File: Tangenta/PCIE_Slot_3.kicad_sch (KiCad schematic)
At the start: 10 parts, among them J20 10018784-10213TLF

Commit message: M2_Slot, PCIE_x16_Slot, PCIE_Switch
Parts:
- J20: footprint PCIE_x16_Slot:PCIE_x16_Slot -> CholaFootprintsPrjLib:PCIE_x16_Slot
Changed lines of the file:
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@@
       (effects (font (size 1.27 1.27)))
     )
-    (property "Footprint" "PCIE_x16_Slot:PCIE_x16_Slot" (at 218.44 154.635 0)
+    (property "Footprint" "CholaFootprintsPrjLib:PCIE_x16_Slot" (at 218.44 154.635 0)
       (effects (font (size 1.27 1.27)) (justify left top) hide)
     )

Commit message: CAP_L6, CAP_TANTAL_A, M24C04-RMN6TP
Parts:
- C114, C115: footprint CAP_L6:CAP_L6 -> CholaFootprintsPrjLib:CAP_L6
- C116, C117: footprint CAP_TANTAL_A:CAP_TANTAL_A -> CholaFootprintsPrjLib:CAP_TANTAL_A
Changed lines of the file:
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@@
       (effects (font (size 1.27 1.27)) (justify right))
     )
-    (property "Footprint" "CAP_TANTAL_A:CAP_TANTAL_A" (at 203.581 260.477 0)
+    (property "Footprint" "CholaFootprintsPrjLib:CAP_TANTAL_A" (at 203.581 260.477 0)
       (effects (font (size 1.27 1.27) italic) hide)
     )
@@
     )
   )
-  (symbol (lib_id "CholaSymbolsPrjLib:35CE47AX") (at 203.2 263.525 0) (unit 1)
+  (symbol (lib_name "35CE47AX_1") (lib_id "CholaSymbolsPrjLib:35CE47AX") (at 203.2 263.525 0) (unit 1)
     (in_bom yes) (on_board yes) (dnp no)
     (property "Reference" "C115" (at 205.105 262.255 0)
@@
       (effects (font (size 1.27 1.27)) (justify left))
     )
-    (property "Footprint" "CAP_L6:CAP_L6" (at 206.248 282.575 0)
+    (property "Footprint" "CholaFootprintsPrjLib:CAP_L6" (at 206.248 282.575 0)
       (effects (font (size 1.27 1.27) italic) hide)
     )
@@
     )
   )
-  (symbol (lib_id "CholaSymbolsPrjLib:CA45-A-6_3V-47UF-K") (at 226.06 263.525 270) (mirror x) (unit 1)
+  (symbol (lib_name "CA45-A-6_3V-47UF-K_1") (lib_id "CholaSymbolsPrjLib:CA45-A-6_3V-47UF-K") (at 226.06 263.525 270) (mirror x) (unit 1)
     (in_bom yes) (on_board yes) (dnp no)
     (property "Reference" "C117" (at 233.68 262.255 90)
@@
       (effects (font (size 1.27 1.27)) (justify right))
     )
-    (property "Footprint" "CAP_TANTAL_A:CAP_TANTAL_A" (at 214.376 260.477 0)
+    (property "Footprint" "CholaFootprintsPrjLib:CAP_TANTAL_A" (at 214.376 260.477 0)
       (effects (font (size 1.27 1.27) italic) hide)
     )
@@
       (effects (font (size 1.27 1.27)) (justify left))
     )
-    (property "Footprint" "CAP_L6:CAP_L6" (at 196.088 282.575 0)
+    (property "Footprint" "CholaFootprintsPrjLib:CAP_L6" (at 196.088 282.575 0)
       (effects (font (size 1.27 1.27) italic) hide)
     )

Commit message: Removing component association with previous project (local) libraries.
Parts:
- C114, C115: footprint CholaFootprintsPrjLib:CAP_L6 -> CAP_L6:CAP_L6; symbol CholaSymbolsPrjLib:35CE47AX -> 35CE47AX:35CE47AX
- C116, C117: footprint CholaFootprintsPrjLib:CAP_TANTAL_A -> CAP_TANTAL_A:CAP_TANTAL_A; symbol CholaSymbolsPrjLib:CA45-A-6_3V-47UF-K -> CA45-A-6_3V-47UF-K:CA45-A-6_3V-47UF-K
- J20: footprint CholaFootprintsPrjLib:PCIE_x16_Slot -> PCIE_x16_Slot:PCIE_x16_Slot; symbol CholaSymbolsPrjLib:10018784-10213TLF -> 10018784-10213TLF:10018784-10213TLF
- R88, R89, R90, R91: symbol CholaSymbolsPrjLib:R_Small_US -> R_Small_US:R_Small_US
- TP3: symbol CholaSymbolsPrjLib:TestPoint_Small -> TestPoint_Small:TestPoint_Small
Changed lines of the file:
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@@
 	)
 	(symbol
-		(lib_id "CholaSymbolsPrjLib:R_Small_US")
+		(lib_id "R_Small_US:R_Small_US")
 		(at 237.49 236.855 270)
 		(unit 1)
@@
 	)
 	(symbol
-		(lib_id "CholaSymbolsPrjLib:R_Small_US")
+		(lib_id "R_Small_US:R_Small_US")
 		(at 237.49 239.395 270)
 		(unit 1)
@@
 	)
 	(symbol
-		(lib_id "CholaSymbolsPrjLib:CA45-A-6_3V-47UF-K")
+		(lib_id "CA45-A-6_3V-47UF-K:CA45-A-6_3V-47UF-K")
 		(at 215.265 263.525 270)
 		(mirror x)
@@
 			)
 		)
-		(property "Footprint" "CholaFootprintsPrjLib:CAP_TANTAL_A"
+		(property "Footprint" "CAP_TANTAL_A:CAP_TANTAL_A"
 			(at 203.581 260.477 0)
 			(effects
@@
 	)
 	(symbol
-		(lib_id "CholaSymbolsPrjLib:10018784-10213TLF")
+		(lib_id "10018784-10213TLF:10018784-10213TLF")
 		(at 196.85 249.555 0)
 		(mirror x)
@@
 			)
 		)
-		(property "Footprint" "CholaFootprintsPrjLib:PCIE_x16_Slot"
+		(property "Footprint" "PCIE_x16_Slot:PCIE_x16_Slot"
 			(at 218.44 154.635 0)
 			(effects
@@
 	)
 	(symbol
-		(lib_id "CholaSymbolsPrjLib:R_Small_US")
+		(lib_id "R_Small_US:R_Small_US")
 		(at 34.29 45.72 270)
 		(unit 1)
@@
 	)
 	(symbol
-		(lib_id "CholaSymbolsPrjLib:R_Small_US")
+		(lib_id "R_Small_US:R_Small_US")
 		(at 241.935 203.2 0)
 		(unit 1)
@@
 	(symbol
 		(lib_name "35CE47AX_1")
-		(lib_id "CholaSymbolsPrjLib:35CE47AX")
+		(lib_id "35CE47AX:35CE47AX")
 		(at 203.2 263.525 0)
 		(unit 1)
@@
 			)
 		)
-		(property "Footprint" "CholaFootprintsPrjLib:CAP_L6"
+		(property "Footprint" "CAP_L6:CAP_L6"
 			(at 206.248 282.575 0)
 			(effects
@@
 	(symbol
 		(lib_name "CA45-A-6_3V-47UF-K_1")
-		(lib_id "CholaSymbolsPrjLib:CA45-A-6_3V-47UF-K")
+		(lib_id "CA45-A-6_3V-47UF-K:CA45-A-6_3V-47UF-K")
 		(at 226.06 263.525 270)
 		(mirror x)
@@
 			)
 		)
-		(property "Footprint" "CholaFootprintsPrjLib:CAP_TANTAL_A"
+		(property "Footprint" "CAP_TANTAL_A:CAP_TANTAL_A"
 			(at 214.376 260.477 0)
 			(effects
@@
 	)
 	(symbol
-		(lib_id "CholaSymbolsPrjLib:TestPoint_Small")
+		(lib_id "TestPoint_Small:TestPoint_Small")
 		(at 245.11 208.915 0)
 		(unit 1)
@@
 	)
 	(symbol
-		(lib_id "CholaSymbolsPrjLib:35CE47AX")
+		(lib_id "35CE47AX:35CE47AX")
 		(at 193.04 263.525 0)
 		(unit 1)
@@
 			)
 		)
-		(property "Footprint" "CholaFootprintsPrjLib:CAP_L6"
+		(property "Footprint" "CAP_L6:CAP_L6"
 			(at 196.088 282.575 0)
 			(effects

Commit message: Fixes, before checks.
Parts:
- C114, C115: symbol 35CE47AX:35CE47AX -> CAP_L6:35CE47AX
- C116, C117: symbol CA45-A-6_3V-47UF-K:CA45-A-6_3V-47UF-K -> CAP_TANTAL_A:CA45-A-6_3V-47UF-K
- J20: symbol 10018784-10213TLF:10018784-10213TLF -> PCIE_x16_Slot:10018784-10213TLF
- R88, R89, R90, R91: symbol R_Small_US:R_Small_US -> Device:R_Small_US
- TP3: symbol TestPoint_Small:TestPoint_Small -> Connector:TestPoint_Small
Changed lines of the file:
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@@
 	)
 	(symbol
-		(lib_id "R_Small_US:R_Small_US")
+		(lib_id "Device:R_Small_US")
 		(at 237.49 236.855 270)
 		(unit 1)
@@
 	)
 	(symbol
-		(lib_id "R_Small_US:R_Small_US")
+		(lib_id "Device:R_Small_US")
 		(at 237.49 239.395 270)
 		(unit 1)
@@
 	)
 	(symbol
-		(lib_id "CA45-A-6_3V-47UF-K:CA45-A-6_3V-47UF-K")
+		(lib_id "CAP_TANTAL_A:CA45-A-6_3V-47UF-K")
 		(at 215.265 263.525 270)
 		(mirror x)
@@
 	)
 	(symbol
-		(lib_id "10018784-10213TLF:10018784-10213TLF")
+		(lib_id "PCIE_x16_Slot:10018784-10213TLF")
 		(at 196.85 249.555 0)
 		(mirror x)
@@
 	)
 	(symbol
-		(lib_id "R_Small_US:R_Small_US")
+		(lib_id "Device:R_Small_US")
 		(at 34.29 45.72 270)
 		(unit 1)
@@
 	)
 	(symbol
-		(lib_id "R_Small_US:R_Small_US")
+		(lib_id "Device:R_Small_US")
 		(at 241.935 203.2 0)
 		(unit 1)
@@
 	(symbol
 		(lib_name "35CE47AX_1")
-		(lib_id "35CE47AX:35CE47AX")
+		(lib_id "CAP_L6:35CE47AX")
 		(at 203.2 263.525 0)
 		(unit 1)
@@
 	(symbol
 		(lib_name "CA45-A-6_3V-47UF-K_1")
-		(lib_id "CA45-A-6_3V-47UF-K:CA45-A-6_3V-47UF-K")
+		(lib_id "CAP_TANTAL_A:CA45-A-6_3V-47UF-K")
 		(at 226.06 263.525 270)
 		(mirror x)
@@
 	)
 	(symbol
-		(lib_id "TestPoint_Small:TestPoint_Small")
+		(lib_id "Connector:TestPoint_Small")
 		(at 245.11 208.915 0)
 		(unit 1)
@@
 	)
 	(symbol
-		(lib_id "35CE47AX:35CE47AX")
+		(lib_id "CAP_L6:35CE47AX")
 		(at 193.04 263.525 0)
 		(unit 1)

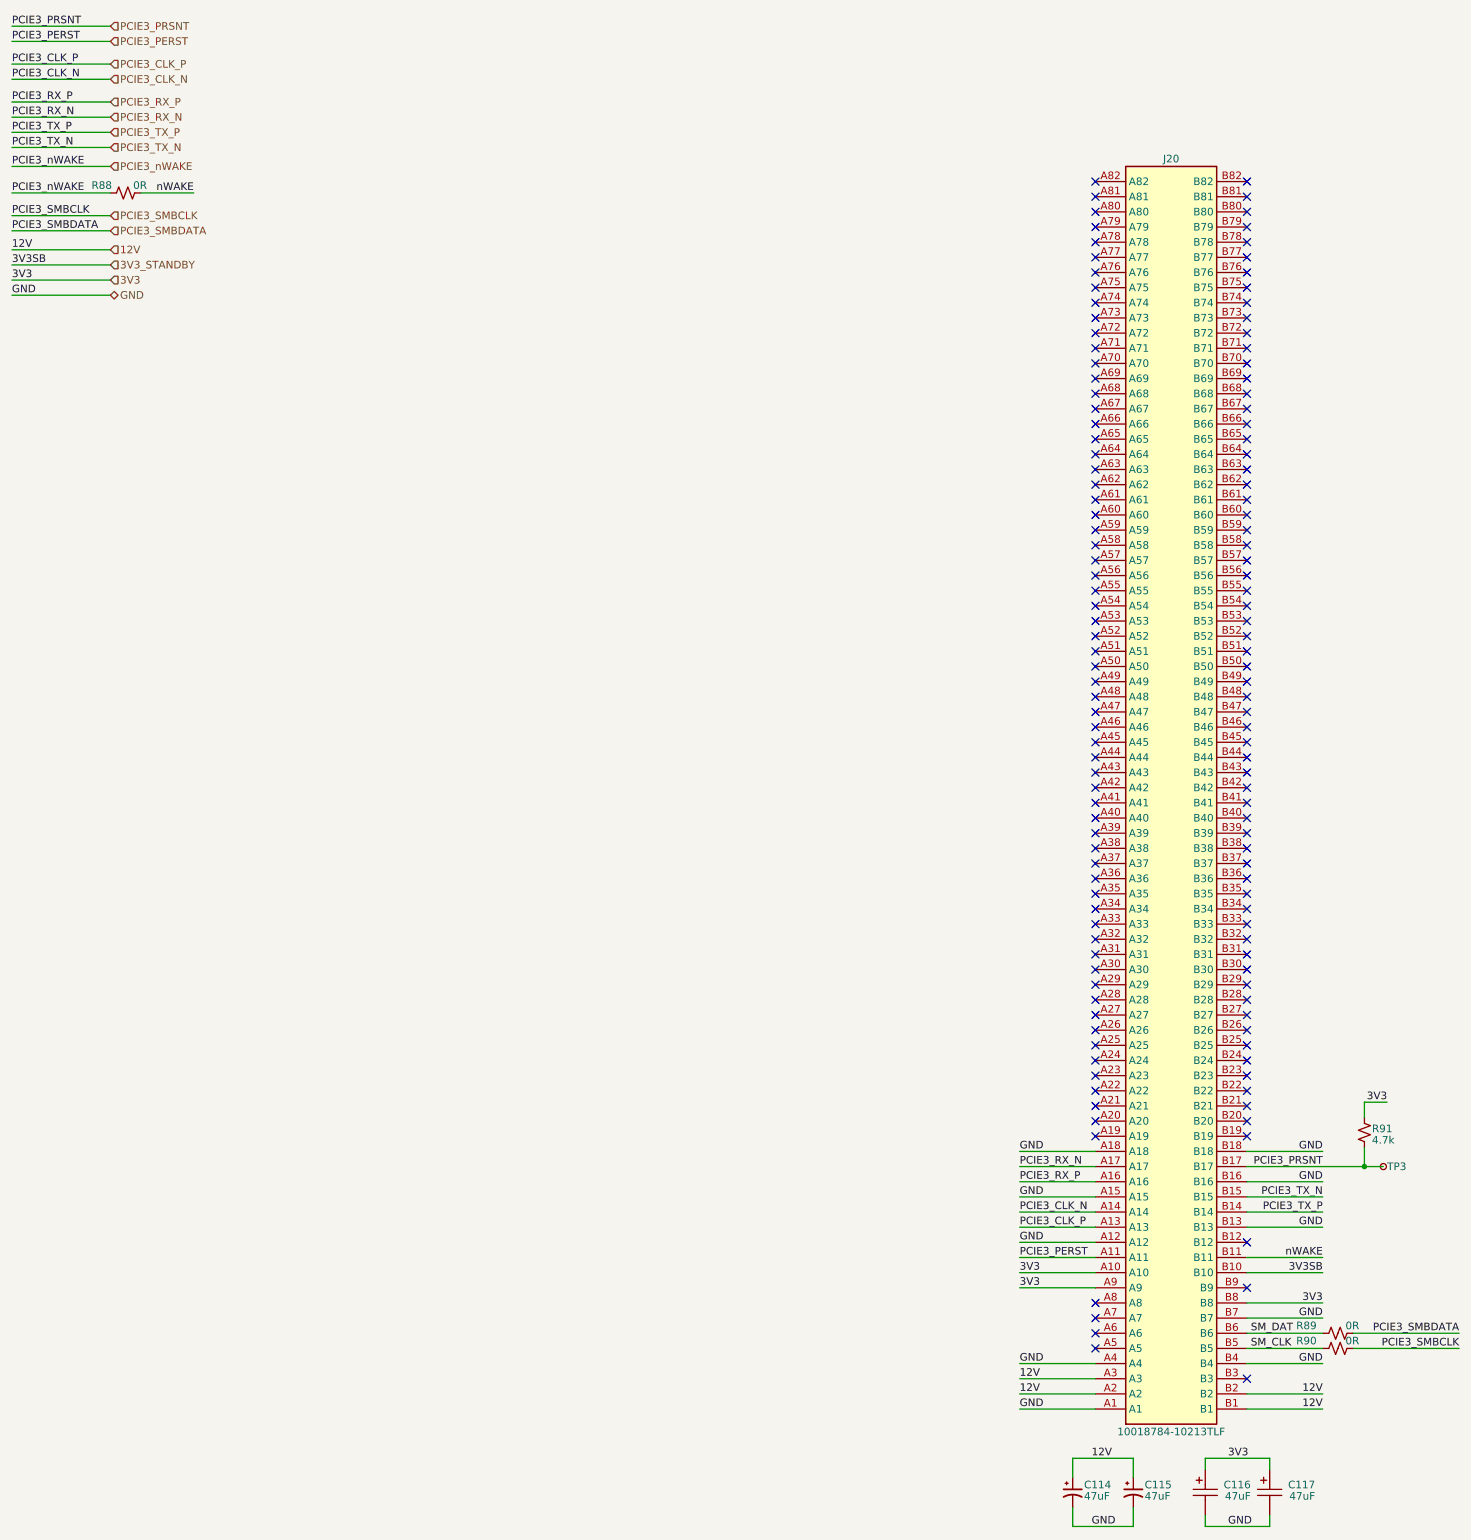
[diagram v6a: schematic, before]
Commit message: Reverting to the original design.
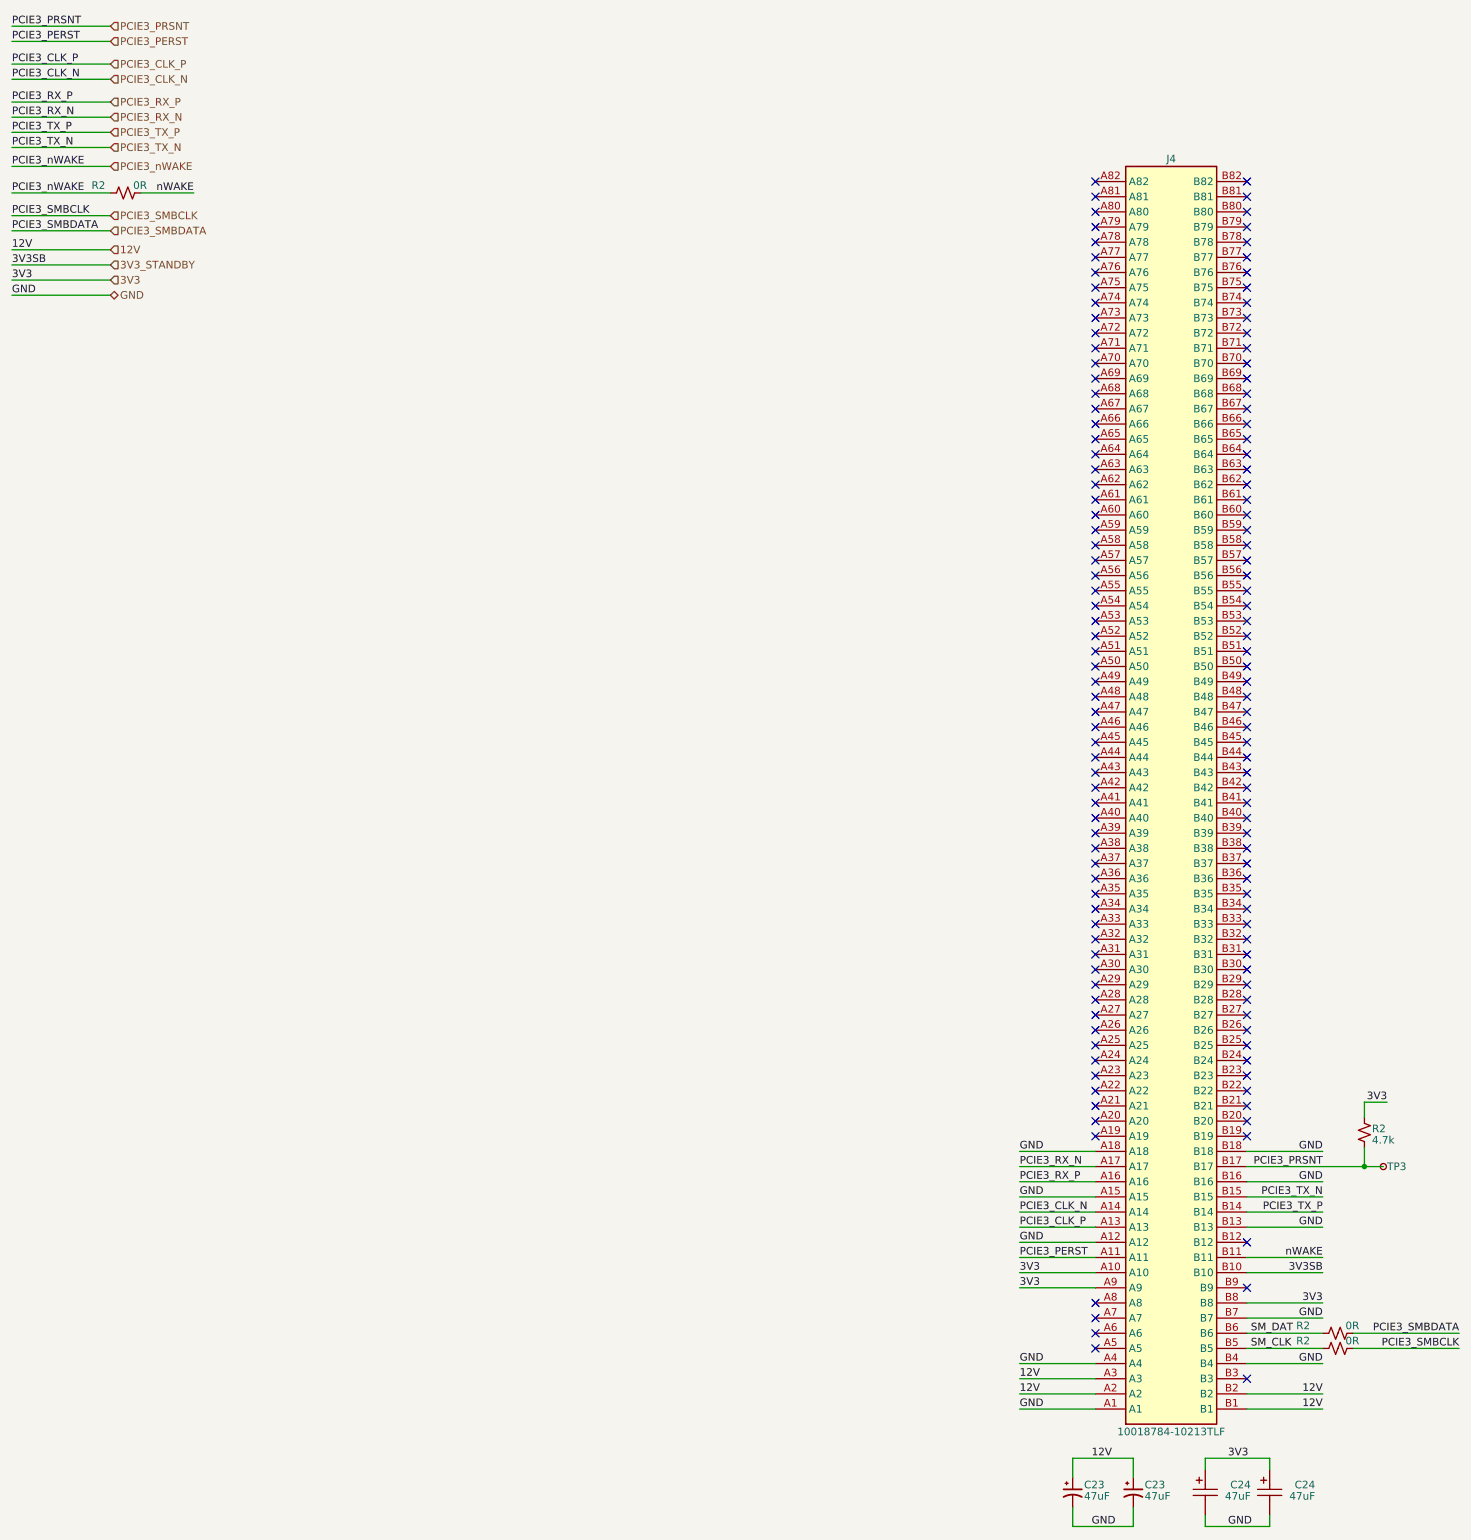
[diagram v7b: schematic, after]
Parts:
- C23: renamed from C115; symbol CAP_L6:35CE47AX -> CholaSymbolsPrjLib:35CE47AX
- C23: renamed from C114; symbol CAP_L6:35CE47AX -> CholaSymbolsPrjLib:35CE47AX
- C24: renamed from C116; symbol CAP_TANTAL_A:CA45-A-6_3V-47UF-K -> CholaSymbolsPrjLib:CA45-A-6_3V-47UF-K
- C24: renamed from C117; symbol CAP_TANTAL_A:CA45-A-6_3V-47UF-K -> CholaSymbolsPrjLib:CA45-A-6_3V-47UF-K
- J4: renamed from J20; symbol PCIE_x16_Slot:10018784-10213TLF -> CholaSymbolsPrjLib:10018784-10213TLF
- R2: renamed from R89; symbol Device:R_Small_US -> CholaSymbolsPrjLib:R_Small_US
- R2: renamed from R90; symbol Device:R_Small_US -> CholaSymbolsPrjLib:R_Small_US
- R2: renamed from R88; symbol Device:R_Small_US -> CholaSymbolsPrjLib:R_Small_US
- R2: renamed from R91; symbol Device:R_Small_US -> CholaSymbolsPrjLib:R_Small_US
- TP3: symbol Connector:TestPoint_Small -> CholaSymbolsPrjLib:TestPoint_Small

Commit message: ...
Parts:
- C23: symbol CholaSymbolsPrjLib:35CE47AX -> LocalPrjLib:35CE47AX
- C24: symbol CholaSymbolsPrjLib:CA45-A-6_3V-47UF-K -> LocalPrjLib:CA45-A-6_3V-47UF-K
- J4: symbol CholaSymbolsPrjLib:10018784-10213TLF -> LocalPrjLib:10018784-10213TLF
- R2: symbol CholaSymbolsPrjLib:R_Small_US -> LocalPrjLib:R_Small_US
- TP3: symbol CholaSymbolsPrjLib:TestPoint_Small -> LocalPrjLib:TestPoint_Small
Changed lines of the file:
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@@
     (effects (font (size 1.27 1.27)) (justify left))
   )
-  (symbol (lib_id "CholaSymbolsPrjLib:R_Small_US") (at 237.49 236.855 270) (unit 1)
+  (symbol (lib_id "LocalPrjLib:R_Small_US") (at 237.49 236.855 270) (unit 1)
     (in_bom yes) (on_board yes) (dnp no)
     (property "Reference" "R2" (at 230.505 235.585 90)
@@
     )
   )
-  (symbol (lib_id "CholaSymbolsPrjLib:R_Small_US") (at 237.49 239.395 270) (unit 1)
+  (symbol (lib_id "LocalPrjLib:R_Small_US") (at 237.49 239.395 270) (unit 1)
     (in_bom yes) (on_board yes) (dnp no)
     (property "Reference" "R2" (at 230.505 238.125 90)
@@
     )
   )
-  (symbol (lib_id "CholaSymbolsPrjLib:CA45-A-6_3V-47UF-K") (at 215.265 263.525 270) (mirror x) (unit 1)
+  (symbol (lib_id "LocalPrjLib:CA45-A-6_3V-47UF-K") (at 215.265 263.525 270) (mirror x) (unit 1)
     (in_bom yes) (on_board yes) (dnp no)
     (property "Reference" "C24" (at 222.885 262.255 90)
@@
     )
   )
-  (symbol (lib_id "CholaSymbolsPrjLib:10018784-10213TLF") (at 196.85 249.555 0) (mirror x) (unit 1)
+  (symbol (lib_id "LocalPrjLib:10018784-10213TLF") (at 196.85 249.555 0) (mirror x) (unit 1)
     (in_bom yes) (on_board yes) (dnp no)
     (property "Reference" "J4" (at 209.55 40.005 0)
@@
     )
   )
-  (symbol (lib_id "CholaSymbolsPrjLib:R_Small_US") (at 34.29 45.72 270) (unit 1)
+  (symbol (lib_id "LocalPrjLib:R_Small_US") (at 34.29 45.72 270) (unit 1)
     (in_bom yes) (on_board yes) (dnp no)
     (property "Reference" "R2" (at 28.575 44.45 90)
@@
     )
   )
-  (symbol (lib_id "CholaSymbolsPrjLib:R_Small_US") (at 241.935 203.2 0) (unit 1)
+  (symbol (lib_id "LocalPrjLib:R_Small_US") (at 241.935 203.2 0) (unit 1)
     (in_bom yes) (on_board yes) (dnp no)
     (property "Reference" "R2" (at 243.205 202.565 0)
@@
     )
   )
-  (symbol (lib_id "CholaSymbolsPrjLib:35CE47AX") (at 203.2 263.525 0) (unit 1)
+  (symbol (lib_id "LocalPrjLib:35CE47AX") (at 203.2 263.525 0) (unit 1)
     (in_bom yes) (on_board yes) (dnp no)
     (property "Reference" "C23" (at 205.105 262.255 0)
@@
     )
   )
-  (symbol (lib_id "CholaSymbolsPrjLib:CA45-A-6_3V-47UF-K") (at 226.06 263.525 270) (mirror x) (unit 1)
+  (symbol (lib_id "LocalPrjLib:CA45-A-6_3V-47UF-K") (at 226.06 263.525 270) (mirror x) (unit 1)
     (in_bom yes) (on_board yes) (dnp no)
     (property "Reference" "C24" (at 233.68 262.255 90)
@@
     )
   )
-  (symbol (lib_id "CholaSymbolsPrjLib:TestPoint_Small") (at 245.11 208.915 0) (unit 1)
+  (symbol (lib_id "LocalPrjLib:TestPoint_Small") (at 245.11 208.915 0) (unit 1)
     (in_bom yes) (on_board yes) (dnp no)
     (property "Reference" "TP3" (at 245.745 208.915 0)
@@
     )
   )
-  (symbol (lib_id "CholaSymbolsPrjLib:35CE47AX") (at 193.04 263.525 0) (unit 1)
+  (symbol (lib_id "LocalPrjLib:35CE47AX") (at 193.04 263.525 0) (unit 1)
     (in_bom yes) (on_board yes) (dnp no)
     (property "Reference" "C23" (at 194.945 262.255 0)
